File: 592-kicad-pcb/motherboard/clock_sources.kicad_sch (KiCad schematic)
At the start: 21 parts, among them J1 U.FL, U1 SN74LVC1G3157DBVR, U2 SMXS-04K, U3 SN74LVC1G3157DBVR, U8 74LVC1T45GW, Y1 Si5351A, Y2 NX3225GA-25.000M-STD-CRG-2

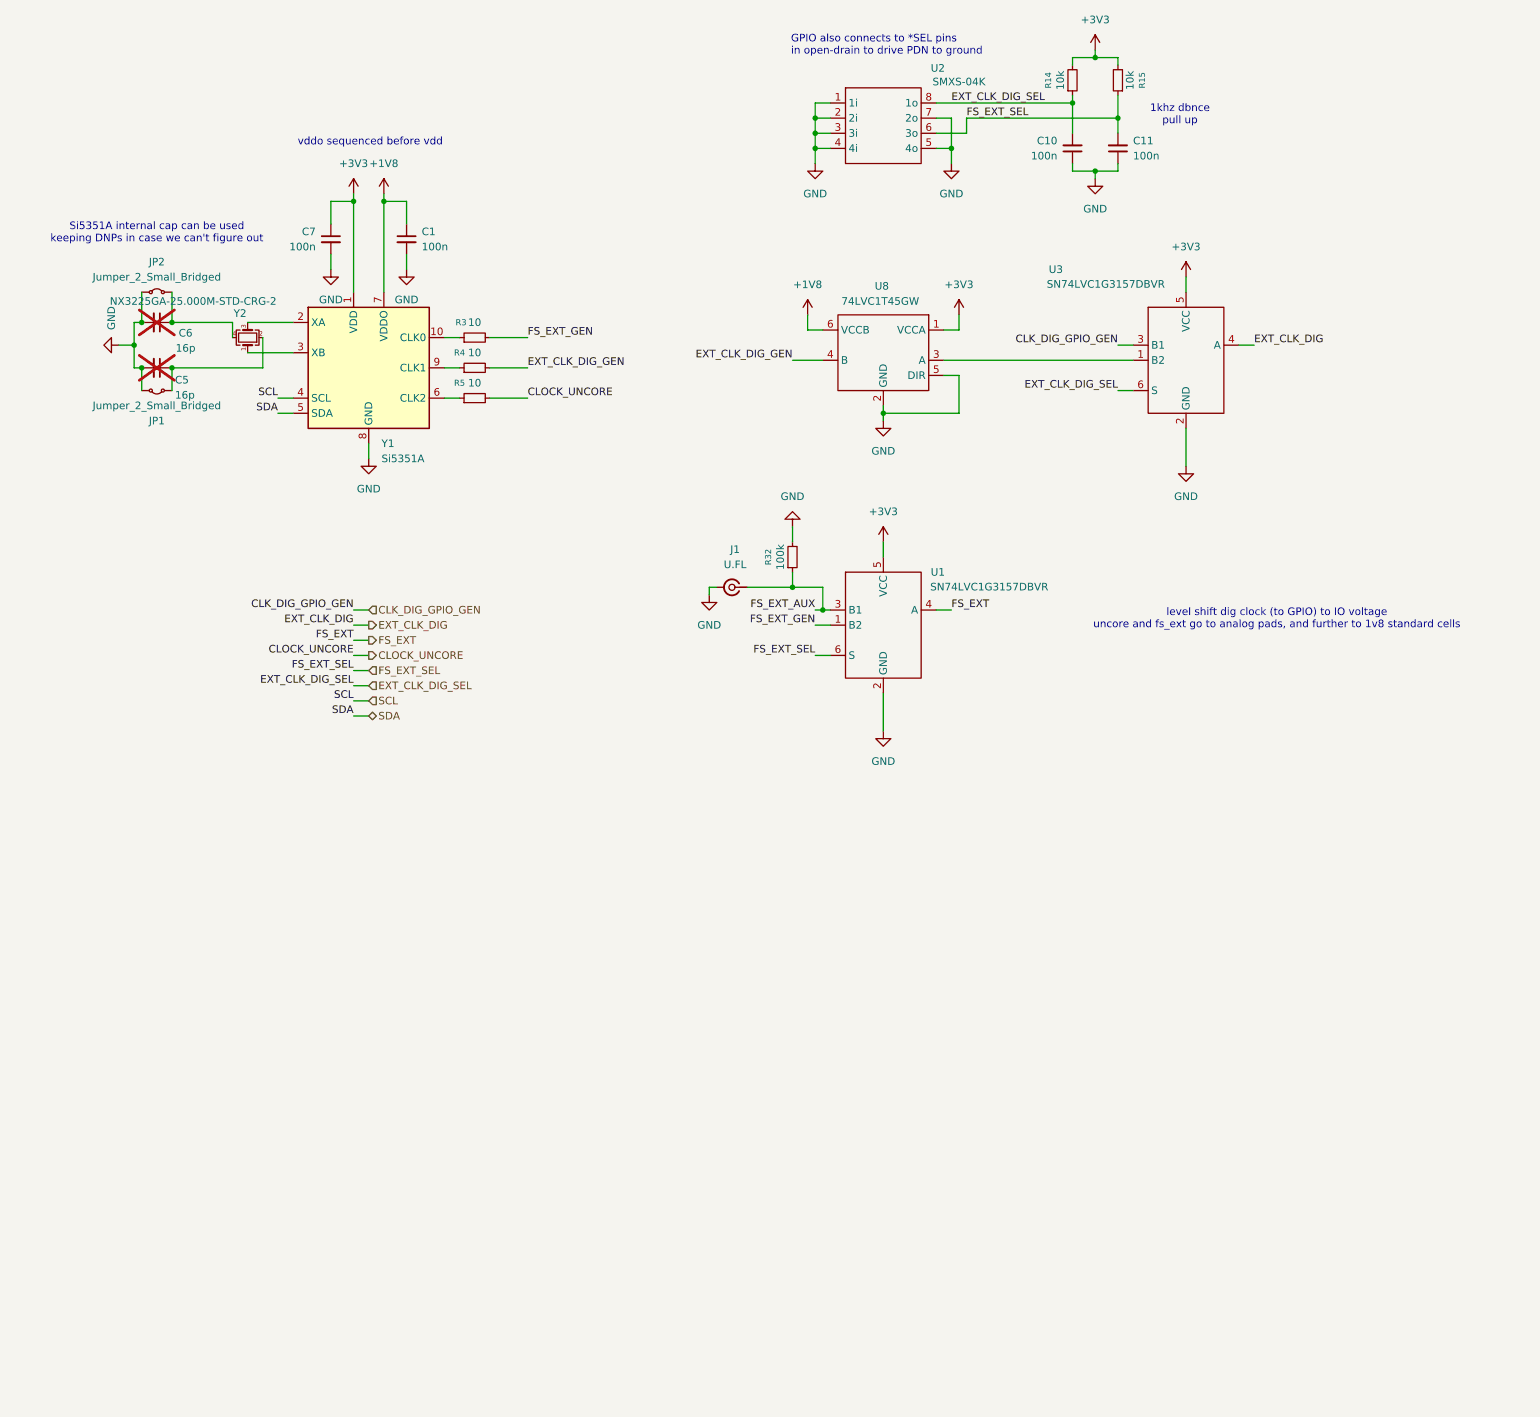
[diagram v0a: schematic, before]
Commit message: clean up schematics, add proper connectors
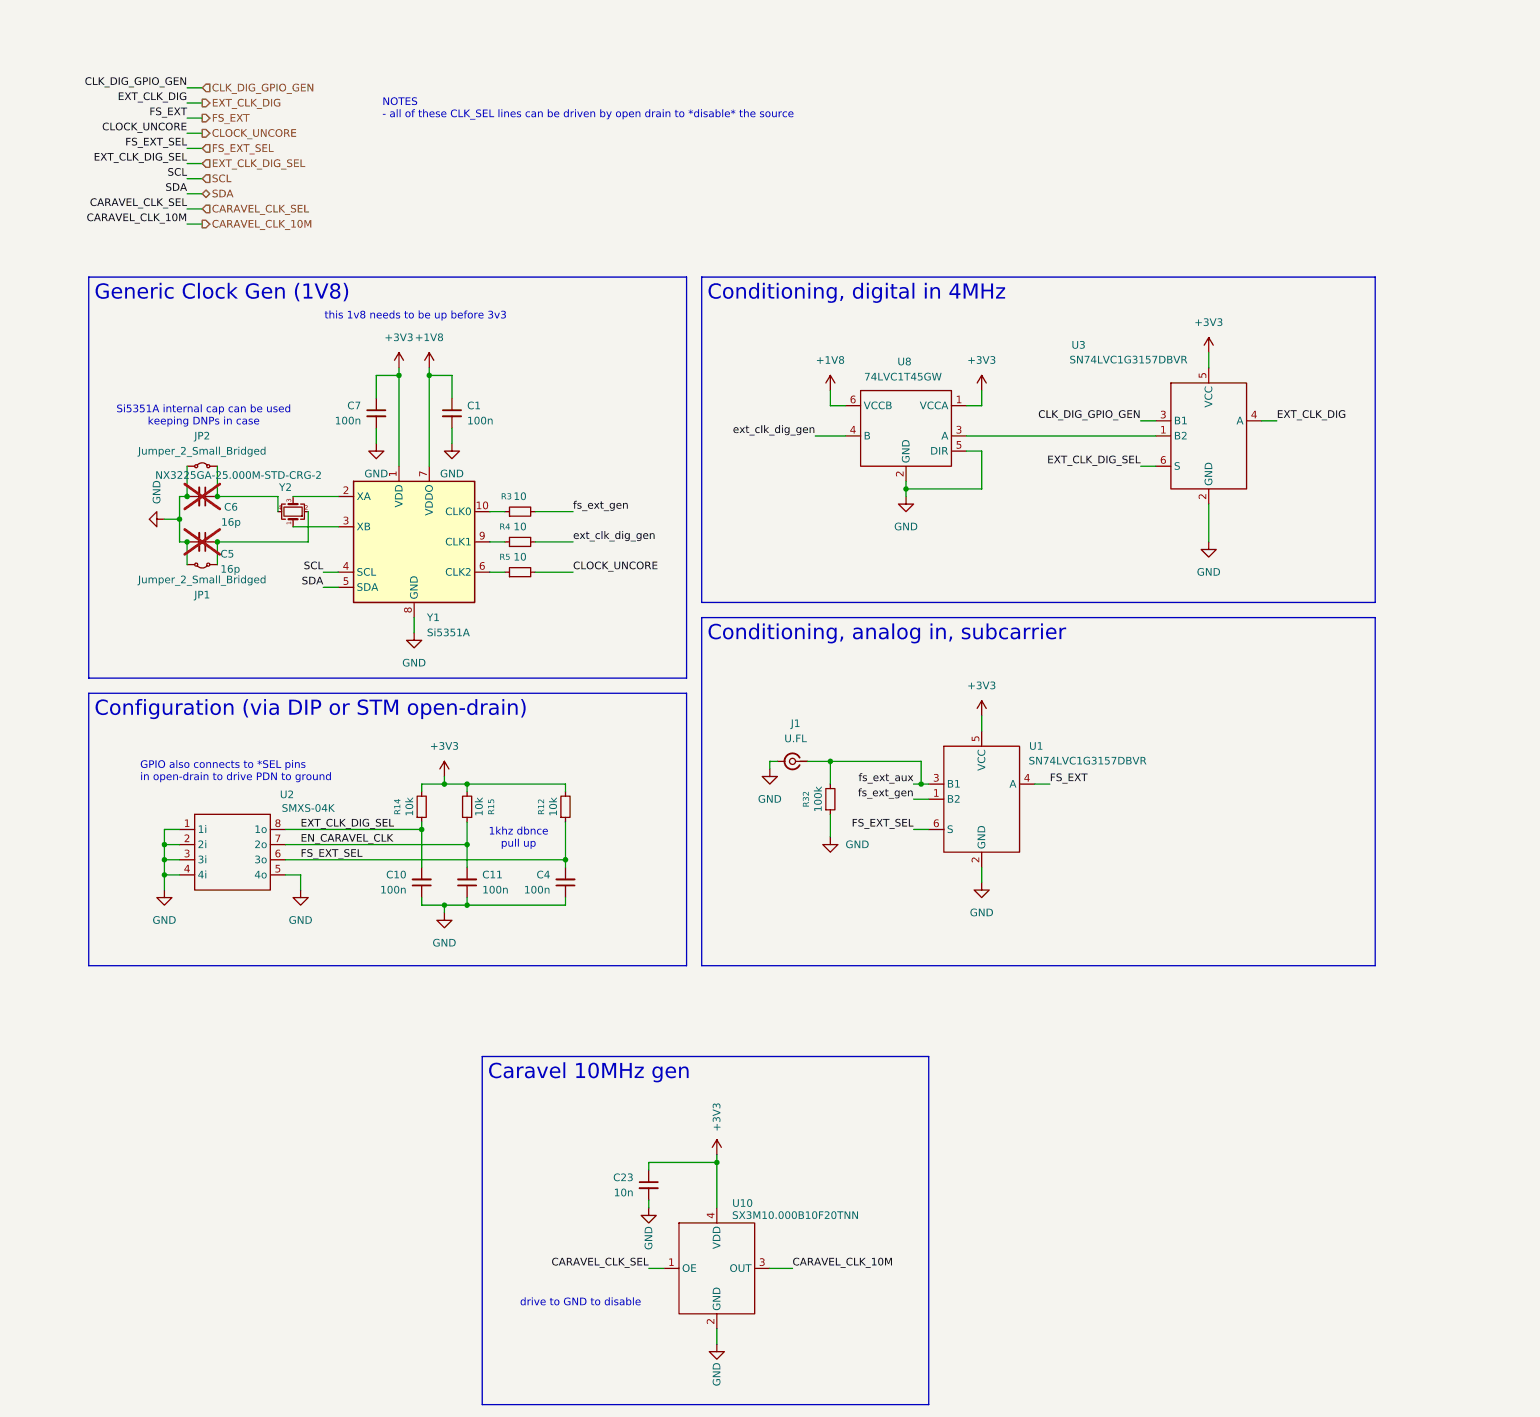
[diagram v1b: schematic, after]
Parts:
- added C23: 10n, Capacitor_SMD:C_0603_1608Metric, symbol Device:C_Small
- added C4: 100n, Capacitor_SMD:C_0603_1608Metric, symbol Device:C_Small
- added R12: 10k, Resistor_SMD:R_0603_1608Metric, symbol Device:R_Small
- added U10: SX3M10.000B10F20TNN, symbol 592-partslib:SX3M10.000B10F20TNN
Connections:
- net +3V3: now also C23.1, R12.2, U10.4 (VDD)
- net FS_EXT_SEL: now also C4.2, R12.1; no longer C11.2, R15.1
- net GND: now also R32.1, C23.2, C4.1, U10.2 (GND); no longer R32.2, U2.7 (2o)
- net EXT_CLK_DIG_GEN renamed ext_clk_dig_gen
- net FS_EXT_AUX renamed fs_ext_aux
- net fs_ext_aux: now also R32.2; no longer R32.1
- net FS_EXT_GEN renamed fs_ext_gen
- new net CARAVEL_CLK_10M: U10.3 (OUT)
- new net CARAVEL_CLK_SEL: U10.1 (OE)
- new net EN_CARAVEL_CLK: C11.2, R15.1, U2.7 (2o)
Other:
- note added: "NOTES - all of these CLK_SEL lines can be driven by open drain to *disable* the source"
- note added: "Si5351A internal cap can be used keeping DNPs in case"
- note added: "drive to GND to disable"
- note added: "this 1v8 needs to be up before 3v3"
- note removed: "Si5351A internal cap can be used keeping DNPs in case we can't figure out"
- note removed: "level shift dig clock (to GPIO) to IO voltage uncore and fs_ext go to analog pads, and further to 1v8 standard cells"
- note removed: "vddo sequenced before vdd"
- moved on the sheet: C1, C10, C11, C5, C6, C7, J1, JP1, JP2, R14, R15, R3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

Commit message: update ftdi chip
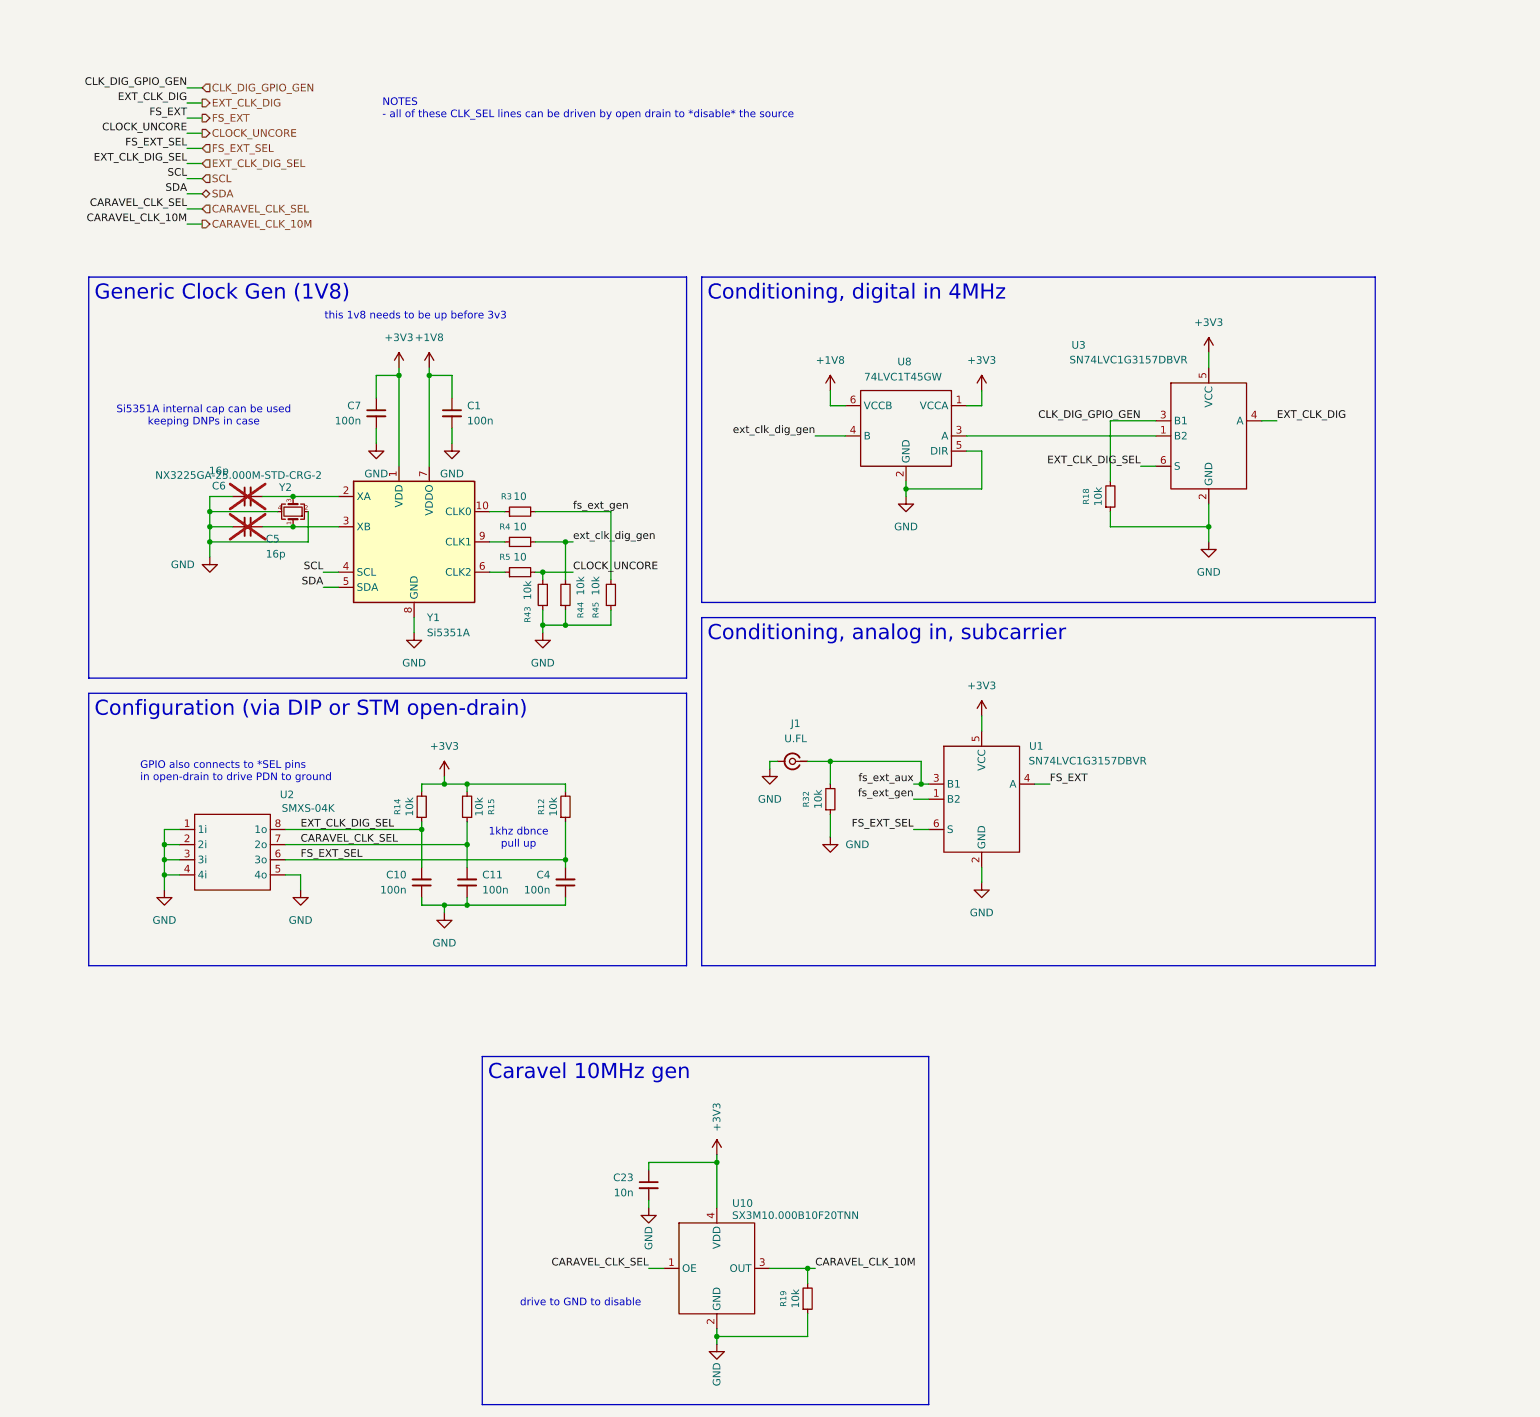
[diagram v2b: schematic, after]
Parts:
- removed JP1, JP2: Jumper_2_Small_Bridged, Jumper:SolderJumper-2_P1.3mm_Bridged_RoundedPad1.0x1.5mm, symbol Jumper:Jumper_2_Small_Bridged
- added R18, R19, R43, R44, R45: 10k, Resistor_SMD:R_0603_1608Metric, symbol Device:R_Small
- R32: value 100k -> 10k
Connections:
- net EN_CARAVEL_CLK is gone; now on net CARAVEL_CLK_SEL: C11.2, R15.1, U2.7 (2o)
- net CARAVEL_CLK_10M: now also R19.2
- net CLK_DIG_GPIO_GEN: now also R18.2
- net CLOCK_UNCORE: now also R43.2
- net GND: now also C6.1, Y2.2, Y2.4, R18.1, R19.1, R43.1, R44.1, R45.1; no longer C6.2
- net ext_clk_dig_gen: now also R44.2
- net fs_ext_gen: now also R45.2
- net at Y1.2 (XA), Y2.3: now also C6.2
- net at Y1.3 (XB), Y2.1: now also C5.1
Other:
- moved on the sheet: C5, C6

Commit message: combine hierarchy of all sans power
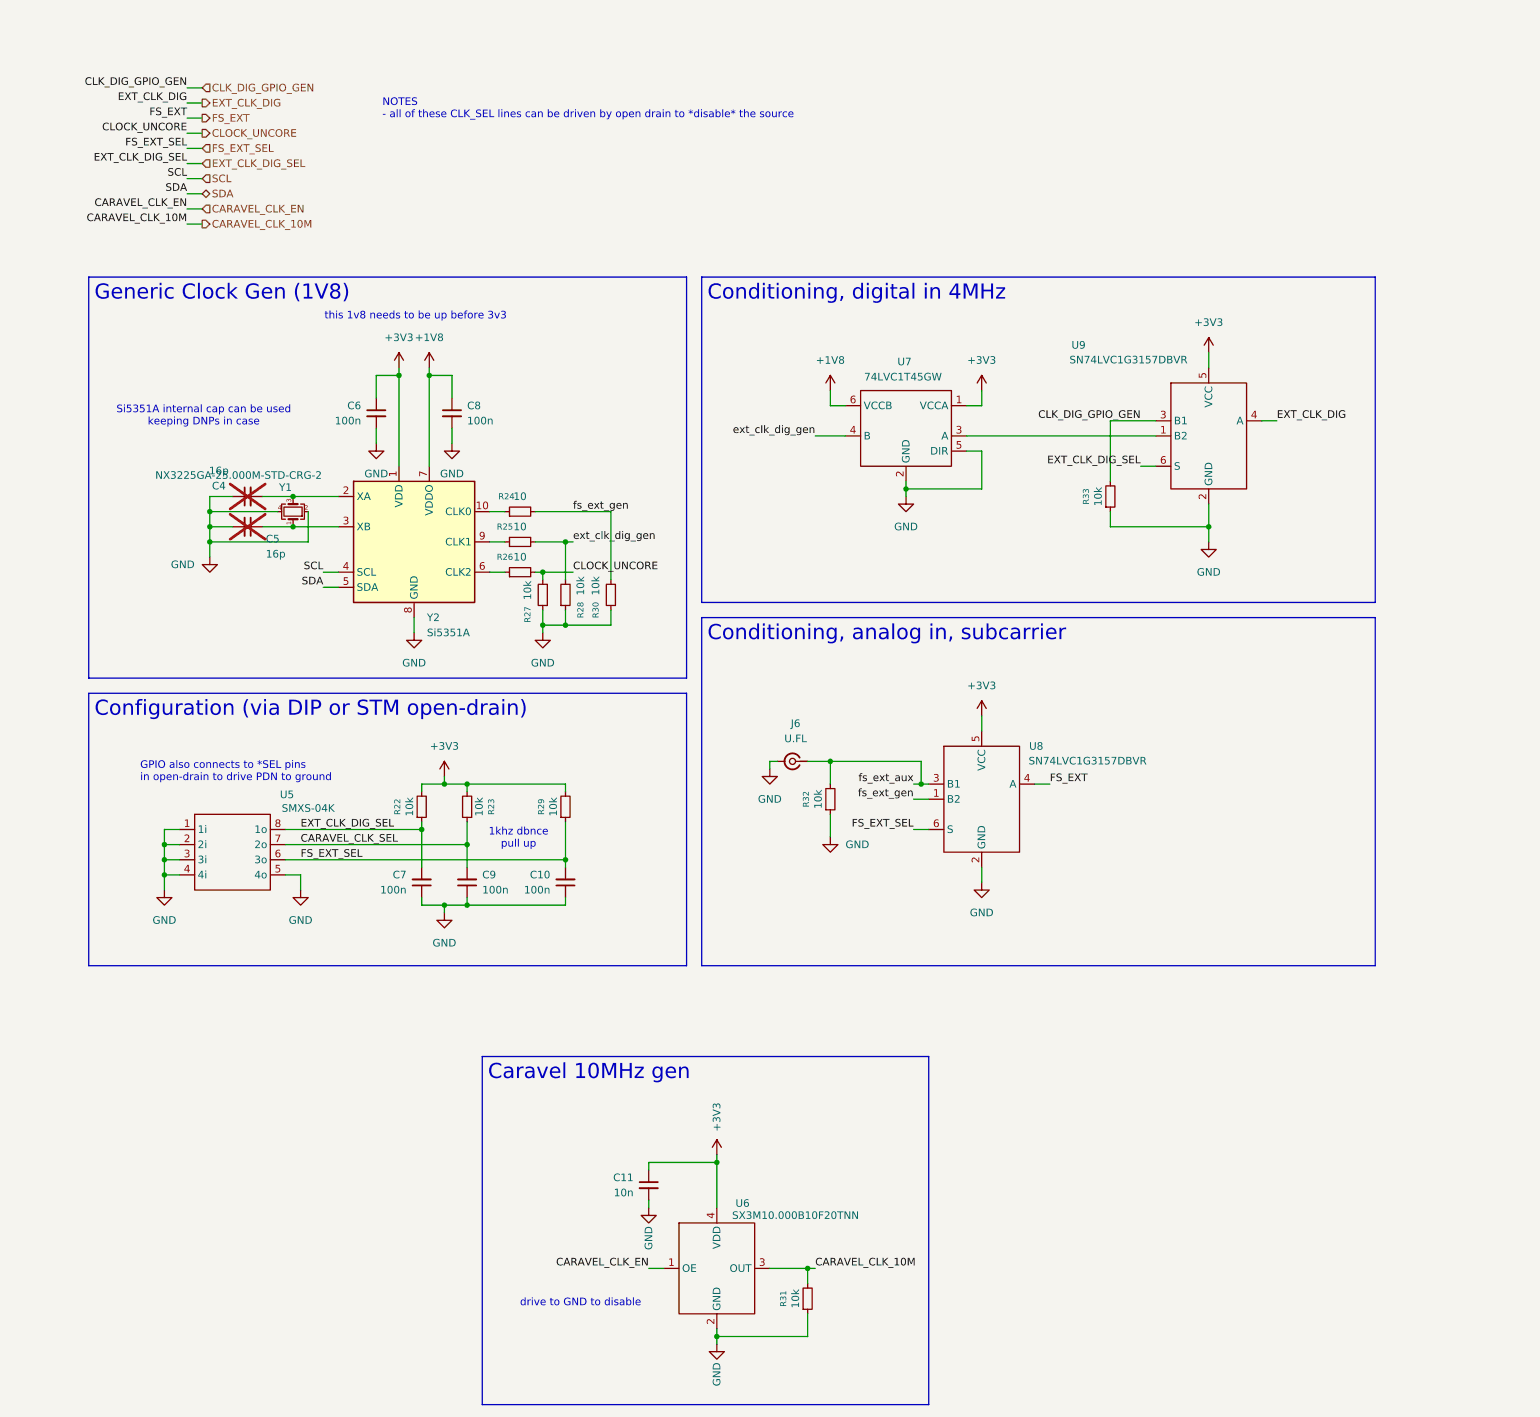
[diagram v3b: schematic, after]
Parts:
- renumbered C4 to C10, C23 to C11, C6 to C4, C7 to C6, C10 to C7, C1 to C8, C11 to C9, J1 to J6, R14 to R22, R15 to R23, R3 to R24, R4 to R25, R5 to R26, R43 to R27, R44 to R28, R12 to R29, R45 to R30, R19 to R31, R18 to R33, U2 to U5, U10 to U6, U8 to U7, U1 to U8, U3 to U9, Y2 to Y1, Y1 to Y2
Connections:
- net CARAVEL_CLK_SEL: no longer U6.1 (OE)
- new net CARAVEL_CLK_EN: U6.1 (OE)
